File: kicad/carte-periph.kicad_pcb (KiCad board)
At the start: 4 copper layers, 33 parts, among them J1 PDB, J2 PWR_IN, J3 PROG, J4 Fix, J5 Fix, J6 Fix, J7 Fix, J8 I2C, J9 I2C, U1 PIC24FJ128GA202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

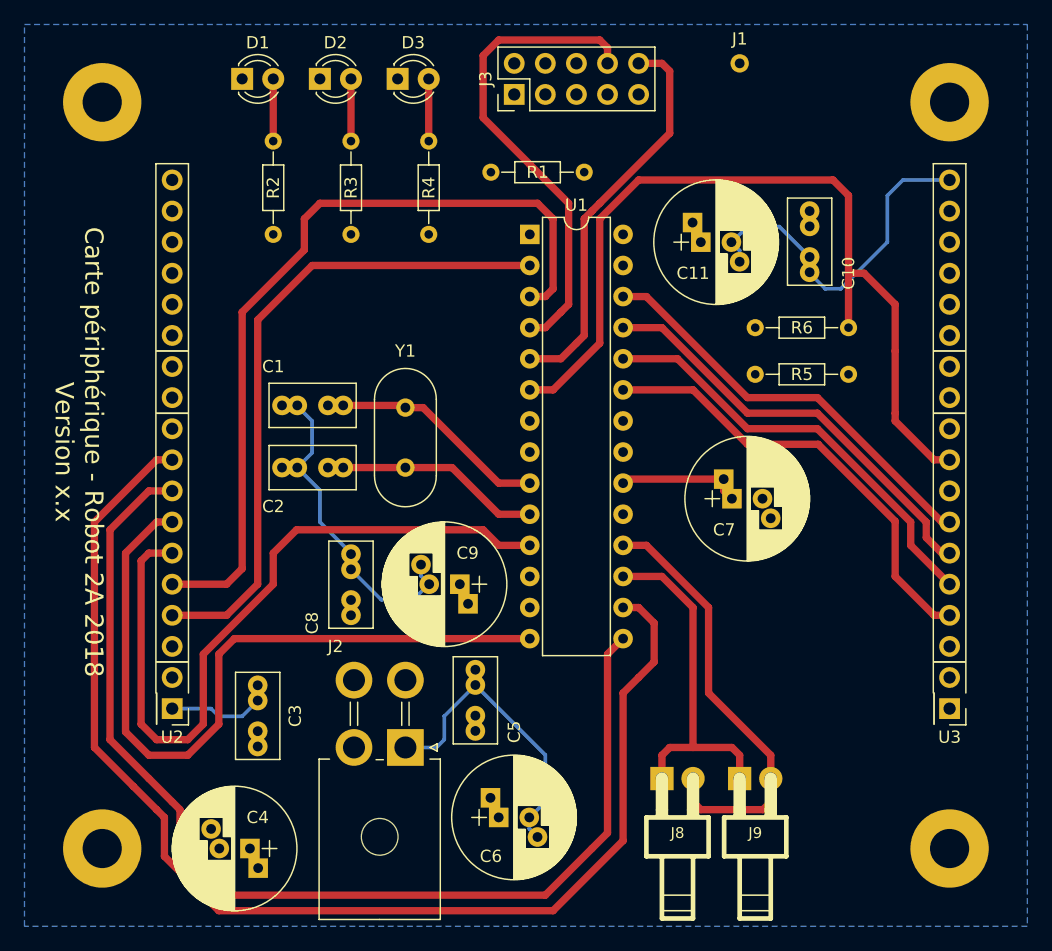
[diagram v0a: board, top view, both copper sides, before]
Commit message: Passage en 2 couches
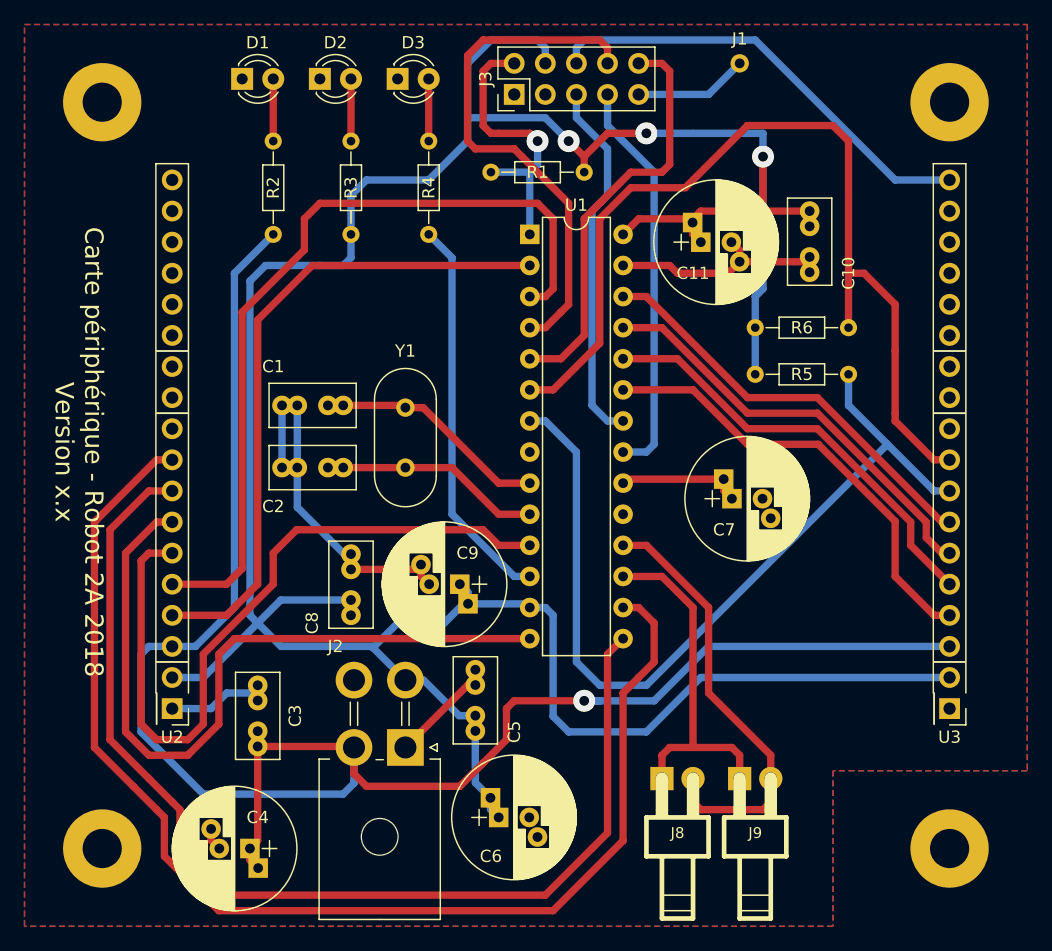
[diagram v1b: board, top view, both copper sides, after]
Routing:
- net +3V3: track 37.8 -> 250.8 mm, vias 0 -> 3
- net GND: track 92.4 -> 105.2 mm
- net +5V: track 139.8 -> 147.8 mm, vias 0 -> 1
- net /I2C_DATA2: track 70.6 -> 76.8 mm
- net /PDT: track 39.4 -> 43.1 mm
- net /RA4: track 33.6 -> 32.1 mm
- net /PCK: track 32.5 -> 34.0 mm
- net /Mclr: track 22.8 -> 24.2 mm, vias 0 -> 1
- added copper zone on F.Cu, net GND
- removed copper zone on In2.Cu, net +3V3
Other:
- copper layers 4 -> 2

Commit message: Enlèvement des résistances de pull up I2C
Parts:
- removed R5, R6: 10k, Resistors_THT:R_Axial_DIN0204_L3.6mm_D1.6mm_P7.62mm_Horizontal
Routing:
- net +3V3: track 250.8 -> 232.7 mm
- net /I2C_CLK2: track 70.0 -> 59.9 mm
- net /I2C_DATA2: track 76.8 -> 72.4 mm
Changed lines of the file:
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@@
 (kicad_pcb (version 4) (host pcbnew 4.0.7)
   (general
-    (links 100)
+    (links 96)
     (no_connects 0)
-    (area 34.925 22.86 116.840001 96.584001)
+    (area 0 0 0 0)
     (thickness 1.6)
     (drawings 9)
-    (tracks 370)
+    (tracks 362)
     (zones 0)
-    (modules 33)
+    (modules 31)
     (nets 52)
   )
@@
     )
   )
-  (module Resistors_THT:R_Axial_DIN0204_L3.6mm_D1.6mm_P7.62mm_Horizontal (layer F.Cu)
-    (at 94.615 51.435)
-    (descr "Resistor, Axial_DIN0204 series, Axial, Horizontal, pin pitch=7.62mm, 0.16666666666666666W = 1/6W, length*diameter=3.6*1.6mm^2, http://cdn-reichelt.de/documents/datenblatt/B400/1_4W%23YAG.pdf")
-    (tags "Resistor Axial_DIN0204 series Axial Horizontal pin pitch 7.62mm 0.16666666666666666W = 1/6W length 3.6mm diameter 1.6mm")
-    (fp_text reference R5 (at 3.81 0) (layer F.SilkS)
-      (effects (font (size 1 1) (thickness 0.15)))
-    )
-    (fp_text value 10k (at 3.81 -1.905) (layer F.Fab)
-      (effects (font (size 1 1) (thickness 0.15)))
-    )
-    (fp_line (start 2.01 -0.8) (end 2.01 0.8) (layer F.Fab) (width 0.1))
-    (fp_line (start 2.01 0.8) (end 5.61 0.8) (layer F.Fab) (width 0.1))
-    (fp_line (start 5.61 0.8) (end 5.61 -0.8) (layer F.Fab) (width 0.1))
-    (fp_line (start 5.61 -0.8) (end 2.01 -0.8) (layer F.Fab) (width 0.1))
-    (fp_line (start 0 0) (end 2.01 0) (layer F.Fab) (width 0.1))
-    (fp_line (start 7.62 0) (end 5.61 0) (layer F.Fab) (width 0.1))
-    (fp_line (start 1.95 -0.86) (end 1.95 0.86) (layer F.SilkS) (width 0.12))
-    (fp_line (start 1.95 0.86) (end 5.67 0.86) (layer F.SilkS) (width 0.12))
-    (fp_line (start 5.67 0.86) (end 5.67 -0.86) (layer F.SilkS) (width 0.12))
-    (fp_line (start 5.67 -0.86) (end 1.95 -0.86) (layer F.SilkS) (width 0.12))
-    (fp_line (start 0.88 0) (end 1.95 0) (layer F.SilkS) (width 0.12))
-    (fp_line (start 6.74 0) (end 5.67 0) (layer F.SilkS) (width 0.12))
-    (fp_line (start -0.95 -1.15) (end -0.95 1.15) (layer F.CrtYd) (width 0.05))
-    (fp_line (start -0.95 1.15) (end 8.6 1.15) (layer F.CrtYd) (width 0.05))
-    (fp_line (start 8.6 1.15) (end 8.6 -1.15) (layer F.CrtYd) (width 0.05))
-    (fp_line (start 8.6 -1.15) (end -0.95 -1.15) (layer F.CrtYd) (width 0.05))
-    (pad 1 thru_hole circle (at 0 0) (size 1.4 1.4) (drill 0.7) (layers *.Cu *.Mask)
-      (net 5 +3V3))
-    (pad 2 thru_hole oval (at 7.62 0) (size 1.4 1.4) (drill 0.7) (layers *.Cu *.Mask)
-      (net 26 /I2C_CLK2))
-    (model ${KISYS3DMOD}/Resistors_THT.3dshapes/R_Axial_DIN0204_L3.6mm_D1.6mm_P7.62mm_Horizontal.wrl
-      (at (xyz 0 0 0))
-      (scale (xyz 0.393701 0.393701 0.393701))
-      (rotate (xyz 0 0 0))
-    )
-  )
-  (module Resistors_THT:R_Axial_DIN0204_L3.6mm_D1.6mm_P7.62mm_Horizontal (layer F.Cu)
-    (at 102.235 47.625 180)
-    (descr "Resistor, Axial_DIN0204 series, Axial, Horizontal, pin pitch=7.62mm, 0.16666666666666666W = 1/6W, length*diameter=3.6*1.6mm^2, http://cdn-reichelt.de/documents/datenblatt/B400/1_4W%23YAG.pdf")
-    (tags "Resistor Axial_DIN0204 series Axial Horizontal pin pitch 7.62mm 0.16666666666666666W = 1/6W length 3.6mm diameter 1.6mm")
-    (fp_text reference R6 (at 3.81 0 180) (layer F.SilkS)
-      (effects (font (size 1 1) (thickness 0.15)))
-    )
-    (fp_text value 10k (at 3.81 1.86 180) (layer F.Fab)
-      (effects (font (size 1 1) (thickness 0.15)))
-    )
-    (fp_line (start 2.01 -0.8) (end 2.01 0.8) (layer F.Fab) (width 0.1))
-    (fp_line (start 2.01 0.8) (end 5.61 0.8) (layer F.Fab) (width 0.1))
-    (fp_line (start 5.61 0.8) (end 5.61 -0.8) (layer F.Fab) (width 0.1))
-    (fp_line (start 5.61 -0.8) (end 2.01 -0.8) (layer F.Fab) (width 0.1))
-    (fp_line (start 0 0) (end 2.01 0) (layer F.Fab) (width 0.1))
-    (fp_line (start 7.62 0) (end 5.61 0) (layer F.Fab) (width 0.1))
-    (fp_line (start 1.95 -0.86) (end 1.95 0.86) (layer F.SilkS) (width 0.12))
-    (fp_line (start 1.95 0.86) (end 5.67 0.86) (layer F.SilkS) (width 0.12))
-    (fp_line (start 5.67 0.86) (end 5.67 -0.86) (layer F.SilkS) (width 0.12))
-    (fp_line (start 5.67 -0.86) (end 1.95 -0.86) (layer F.SilkS) (width 0.12))
-    (fp_line (start 0.88 0) (end 1.95 0) (layer F.SilkS) (width 0.12))
-    (fp_line (start 6.74 0) (end 5.67 0) (layer F.SilkS) (width 0.12))
-    (fp_line (start -0.95 -1.15) (end -0.95 1.15) (layer F.CrtYd) (width 0.05))
-    (fp_line (start -0.95 1.15) (end 8.6 1.15) (layer F.CrtYd) (width 0.05))
-    (fp_line (start 8.6 1.15) (end 8.6 -1.15) (layer F.CrtYd) (width 0.05))
-    (fp_line (start 8.6 -1.15) (end -0.95 -1.15) (layer F.CrtYd) (width 0.05))
-    (pad 1 thru_hole circle (at 0 0 180) (size 1.4 1.4) (drill 0.7) (layers *.Cu *.Mask)
-      (net 27 /I2C_DATA2))
-    (pad 2 thru_hole oval (at 7.62 0 180) (size 1.4 1.4) (drill 0.7) (layers *.Cu *.Mask)
-      (net 5 +3V3))
-    (model ${KISYS3DMOD}/Resistors_THT.3dshapes/R_Axial_DIN0204_L3.6mm_D1.6mm_P7.62mm_Horizontal.wrl
-      (at (xyz 0 0 0))
-      (scale (xyz 0.393701 0.393701 0.393701))
-      (rotate (xyz 0 0 0))
-    )
-  )
   (module conn_shield:conn_shield (layer F.Cu)
     (at 46.99 78.74 180)
@@
   (via (at 85.725 31.75) (size 1.8) (drill 0.8) (layers F.Cu B.Cu) (net 5))
   (segment (start 83.185 31.75) (end 85.725 31.75) (width 0.6) (layer F.Cu) (net 5))
-  (segment (start 94.615 47.625) (end 94.615 51.435) (width 0.6) (layer B.Cu) (net 5))
   (segment (start 95.25 38.1) (end 95.25 33.655) (width 0.6) (layer F.Cu) (net 5))
-  (segment (start 94.615 45.085) (end 94.615 47.625) (width 0.6) (layer B.Cu) (net 5))
-  (segment (start 95.25 44.45) (end 94.615 45.085) (width 0.6) (layer B.Cu) (net 5))
-  (segment (start 95.25 33.655) (end 95.25 44.45) (width 0.6) (layer B.Cu) (net 5))
   (via (at 95.25 33.655) (size 1.8) (drill 0.8) (layers F.Cu B.Cu) (net 5))
   (segment (start 71.155937 70.18) (end 75.895 70.18) (width 0.6) (layer B.Cu) (net 5))
@@
   (segment (start 69.85 62.865) (end 69.85 41.91) (width 0.6) (layer B.Cu) (net 25))
   (segment (start 74.93 67.945) (end 69.85 62.865) (width 0.6) (layer B.Cu) (net 25))
+  (segment (start 110.49 60.96) (end 101.6 60.96) (width 0.6) (layer B.Cu) (net 26) (status 400000))
   (segment (start 78.74 56.515) (end 80.01 57.785) (width 0.6) (layer B.Cu) (net 26))
+  (segment (start 77.47 55.245) (end 76.2 55.245) (width 0.6) (layer B.Cu) (net 26))
+  (segment (start 85.725 76.835) (end 101.6 60.96) (width 0.6) (layer B.Cu) (net 26))
+  (segment (start 81.915 76.835) (end 85.725 76.835) (width 0.6) (layer B.Cu) (net 26))
+  (segment (start 77.47 55.245) (end 78.74 56.515) (width 0.6) (layer B.Cu) (net 26))
+  (segment (start 80.01 57.785) (end 80.01 74.93) (width 0.6) (layer B.Cu) (net 26))
   (segment (start 80.01 74.93) (end 81.915 76.835) (width 0.6) (layer B.Cu) (net 26))
-  (segment (start 80.01 57.785) (end 80.01 74.93) (width 0.6) (layer B.Cu) (net 26))
-  (segment (start 105.41 57.15) (end 102.235 53.975) (width 0.6) (layer B.Cu) (net 26))
-  (segment (start 102.235 53.975) (end 102.235 51.435) (width 0.6) (layer B.Cu) (net 26))
-  (segment (start 110.49 60.96) (end 109.22 60.96) (width 0.6) (layer B.Cu) (net 26))
-  (segment (start 77.47 55.245) (end 78.74 56.515) (width 0.6) (layer B.Cu) (net 26))
-  (segment (start 81.915 76.835) (end 85.725 76.835) (width 0.6) (layer B.Cu) (net 26))
-  (segment (start 85.725 76.835) (end 105.41 57.15) (width 0.6) (layer B.Cu) (net 26))
-  (segment (start 77.47 55.245) (end 76.2 55.245) (width 0.6) (layer B.Cu) (net 26))
-  (segment (start 109.22 60.96) (end 105.41 57.15) (width 0.6) (layer B.Cu) (net 26))
   (segment (start 84.455 36.195) (end 88.9 36.195) (width 0.6) (layer F.Cu) (net 27))
   (segment (start 88.9 36.195) (end 93.98 31.115) (width 0.6) (layer F.Cu) (net 27))
@@
   (segment (start 78.105 52.705) (end 81.915 48.895) (width 0.6) (layer F.Cu) (net 27))
   (segment (start 102.235 36.83) (end 102.235 43.18) (width 0.6) (layer F.Cu) (net 27))
-  (segment (start 102.235 43.18) (end 102.235 47.625) (width 0.6) (layer F.Cu) (net 27))
   (segment (start 81.915 38.735) (end 84.455 36.195) (width 0.6) (layer F.Cu) (net 27))
   (segment (start 81.915 48.895) (end 81.915 38.735) (width 0.6) (layer F.Cu) (net 27))

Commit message: Mise au propre
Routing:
- net /I2C_CLK2: track 59.9 -> 66.2 mm
- net +5V: track 147.8 -> 145.1 mm
- net /RA1: track 66.2 -> 63.9 mm
- net +3V3: track 232.7 -> 230.7 mm
- net /RA4: track 32.1 -> 34.0 mm
- net /RA0: track 53.7 -> 51.8 mm
- net /I2C_CLK1: track 28.9 -> 28.1 mm

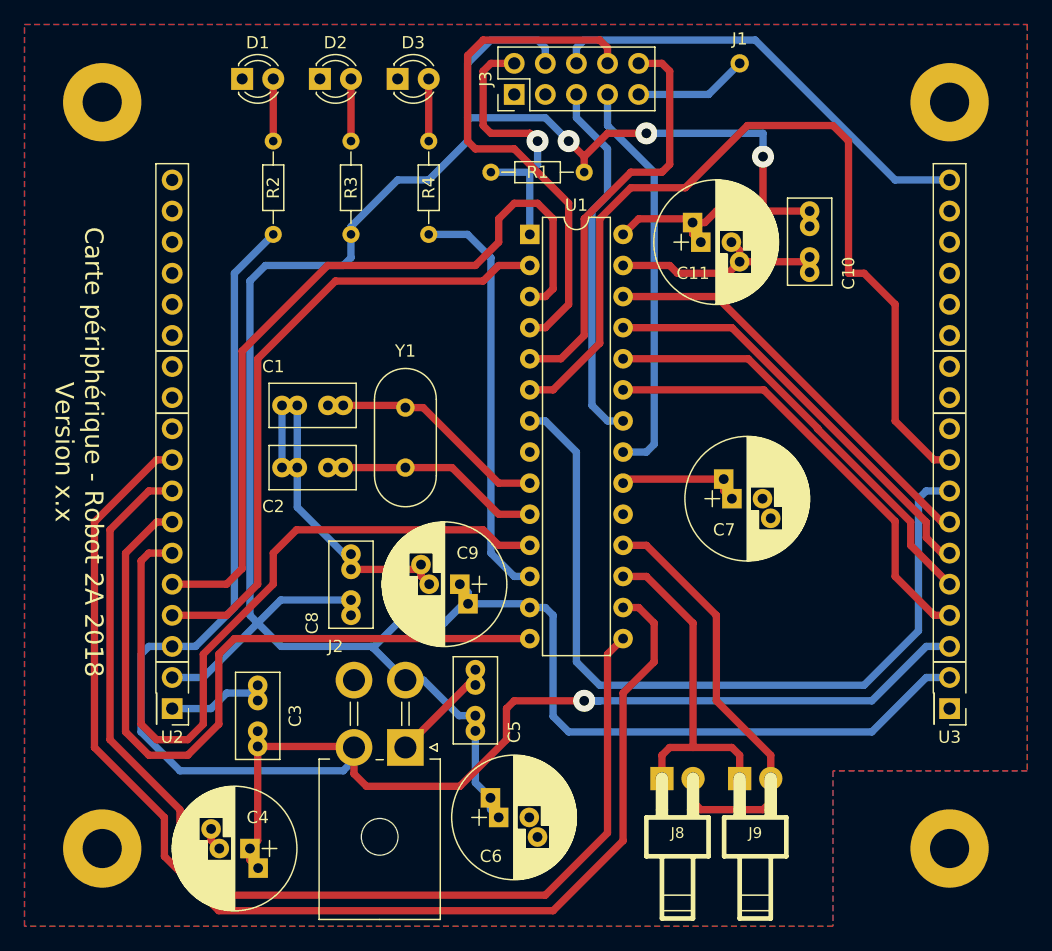
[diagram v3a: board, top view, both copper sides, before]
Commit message: Changement du PIC et rajout d'une empreinte de connecteur
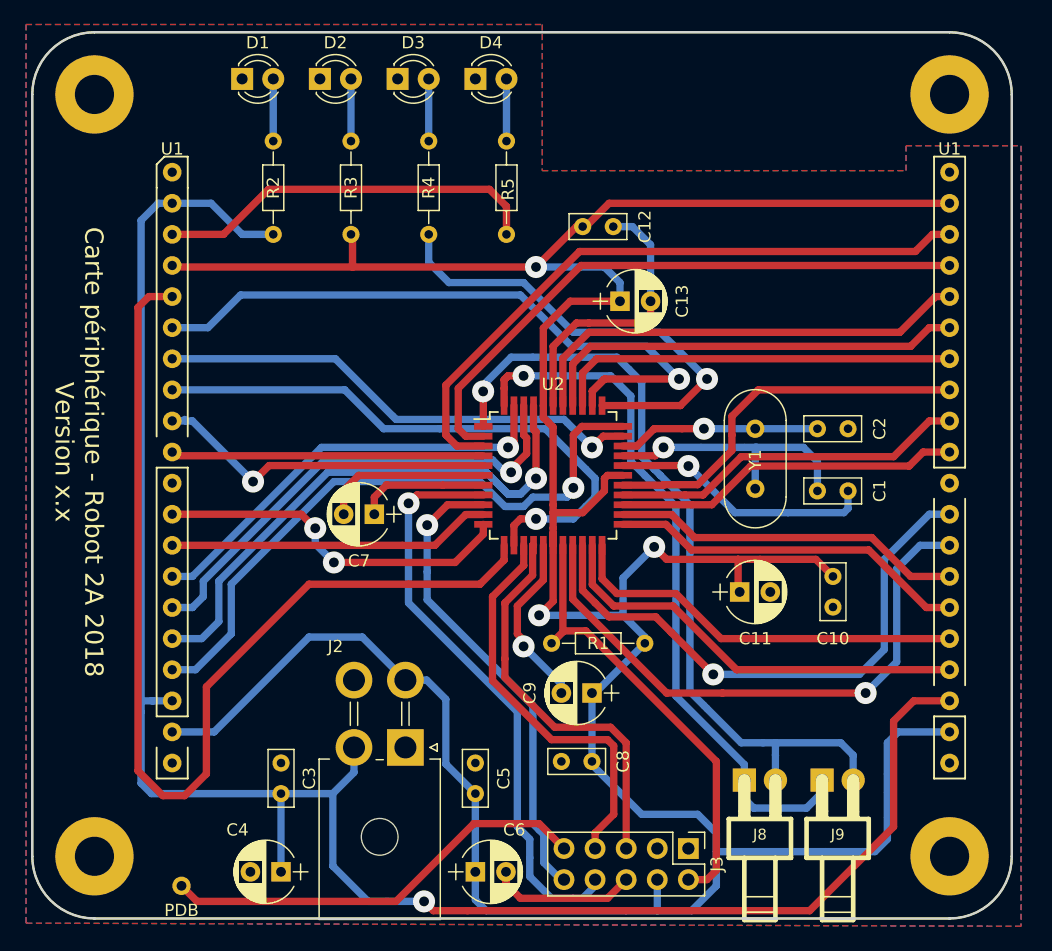
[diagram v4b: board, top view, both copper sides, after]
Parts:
- removed J4, J5, J6, J7: Fix, Mounting_Holes:MountingHole_3.2mm_M3_Pad
- removed U3: Shield_droit, conn_shield:conn_shield
- added C12: 100n, Capacitors_THT:C_Rect_L4.6mm_W2.0mm_P2.50mm_MKS02_FKP02, F.Cu at (80.5, 39.4)
- added C13: 1u, Capacitors_THT:CP_Radial_D5.0mm_P2.50mm, F.Cu at (83.6, 45.5)
- added D4: RED, LEDs:LED_D3.0mm, F.Cu at (71.8, 27.3)
- added R5: 470, Resistors_THT:R_Axial_DIN0204_L3.6mm_D1.6mm_P7.62mm_Horizontal, F.Cu at (74.3, 32.4)
- C1, C10, C2, C3, C5, C8: footprint Capacitors_THT:C_Rect_L7.0mm_W3.5mm_P2.50mm_P5.00mm -> Capacitors_THT:C_Rect_L4.6mm_W2.0mm_P2.50mm_MKS02_FKP02
- C11, C4, C6, C7, C9: footprint Capacitors_THT:CP_Radial_D10.0mm_P2.50mm_P5.00mm -> Capacitors_THT:CP_Radial_D5.0mm_P2.50mm
- U1: value PIC24FJ128GA202 -> Conn_periph; footprint Housings_DIP:DIP-28_W7.62mm -> conn_periph:conn_periph
- U2: value Shield_gauche -> PIC24FJ128GA104; footprint conn_shield:conn_shield -> Housings_QFP:TQFP-44_10x10mm_Pitch0.8mm
- moved J1 81.2 mm to (47.8, 93.2)
- moved J3 63.2 mm to (89.2, 90.2), turned to 270 degrees
- moved U1 52.1 mm to (47.0, 83.2)
- moved C1 39.4 mm to (99.7, 61.0), turned to 0 degrees
- moved C2 38.9 mm to (99.7, 55.9), turned to 0 degrees
- moved R1 38.8 mm to (78.0, 73.4)
- moved U2 36.5 mm to (78.1, 59.7), turned to 0 degrees
- moved C10 29.9 mm to (101.0, 67.9)
- moved C7 29.2 mm to (63.5, 62.9), turned to 180 degrees
- moved C11 28.8 mm to (93.3, 69.2)
- moved Y1 28.8 mm to (94.6, 55.9), turned to 270 degrees
- moved C8 23.0 mm to (81.3, 83.1), turned to 180 degrees
- moved C9 14.0 mm to (81.3, 77.5)
- moved C5 7.62 mm to (71.8, 83.2)
- moved J9 6.73 mm to (101.3, 84.6)
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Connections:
- J2 pad 4: Net-(J2-Pad4) -> (no net)
- J3 pad 1: Net-(J3-Pad1) -> (no net)
- J3 pad 3: Net-(J3-Pad3) -> (no net)
- U2 pad 1: GND -> /I2C_DATA1
- U2 pad 10: GND -> /RB12
- U2 pad 11: /RA7 -> /RB13
- U2 pad 12: /RA8 -> /RA10
- U2 pad 13: /RA9 -> /RA7
- U2 pad 14: /RA10 -> /DEBUG_RX
- U2 pad 15: /RC0 -> /DEBUG_TX
- U2 pad 16: /RC1 -> GND
- U2 pad 17: /RC2 -> +3V3
- U2 pad 18: GND -> /Mclr
- U2 pad 2: +3V3 -> /RC6
- U2 pad 3: +5V -> /RC7
- U2 pad 4: /RA0 -> /RC8
- U2 pad 5: /RA1 -> /RC9
- U2 pad 6: /RB4 -> GND
- U2 pad 7: /RB5 -> Net-(C7-Pad1)
- U2 pad 8: /RB6 -> /PDT
- U2 pad 9: /RB7 -> /PCK
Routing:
- net /RA10: track 0.00 -> 85.1 mm
- net /I2C_DATA2: track 72.4 -> 0.00 mm
- net /RB7: track 101.7 -> 35.4 mm, vias 0 -> 1
- net /I2C_CLK2: track 66.2 -> 0.00 mm
- net /RA9: track 0.00 -> 55.4 mm, vias 0 -> 1
- net /RC7: track 0.00 -> 53.8 mm
- net /RB6: track 90.3 -> 39.9 mm, vias 0 -> 1
- net /RC6: track 0.00 -> 49.9 mm
- net /RA7: track 0.00 -> 48.3 mm, vias 0 -> 1
- net +3V3: track 230.7 -> 277.8 mm
- net /RA8: track 0.00 -> 40.2 mm, vias 0 -> 1
- net /RC5: track 0.00 -> 37.5 mm
- net /RC4: track 0.00 -> 35.4 mm
- net /RB0: track 0.00 -> 35.3 mm
- net /RB14: track 35.0 -> 0.00 mm
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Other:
- board outline added: 80 x 72.4 mm
- net class Default: clearance 0.254 -> 0.127
- rule trace_clearance: 0.254 -> 0.127

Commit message: Validation carte, à passer en release
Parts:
- removed D4: RED, LEDs:LED_D3.0mm
- removed R5: 470, Resistors_THT:R_Axial_DIN0204_L3.6mm_D1.6mm_P7.62mm_Horizontal
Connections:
- U1 pad L1: Net-(R5-Pad2) -> (no net)
- U1 pad V34: +3V3 -> (no net)
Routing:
- net Net-(R5-Pad2): track 31.7 -> 0.00 mm
- net +3V3: track 277.8 -> 261.0 mm
- net Net-(D4-Pad2): track 5.08 -> 0.00 mm
- net /RC9: track 28.1 -> 29.6 mm
- net GND: track 85.9 -> 84.9 mm
- net /PDT: track 48.5 -> 48.0 mm
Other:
- board text added: "CLK"
- board text added: "DATA"
